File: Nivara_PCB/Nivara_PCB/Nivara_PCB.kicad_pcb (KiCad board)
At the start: 4 copper layers, 98.8 x 81.2 mm, 167 parts, among them CN1 ANALOG_IN, CN2 RELAY, J1 AUXILIAR, K1 SRA-24VDC-CL, K2 SRA-24VDC-CL, P1 NPN_IN, P2 PNP_IN, P3 D_IN, P4 RUN/STOP, P5 NPN_OUT, P6 PNP_OUT, P7 RS485, P8 ANALOG_OUT., Q1 IRLML0040, Q2 AO3407A, Q3 IRLML0040, Q4 AO3407A, Q5 IRLML6402TRPBF-JSM, SW1 SKRPACE010, SW2 SKRPACE010, U1 2.54-2*2, U10 GP8201S-TC50-EW, U11 LK1802, U12 LTV-357T, U13 LTV-357T, U14 LTV-357T, U15 LTV-357T, U16 LTV-357T, U17 LTV-357T, U18 LTV-357T, U19 GP8303-TC50-EW, U2 FUENTE IN, U20 FUENTE EX, U3 ESP32-S3-WROOM-1, U4 AP63200WU, U5 RSM3485ECHT_C2992406, U6 LTV-357T, U7 LTV-357T, U8 LTV-357T, U9 LTV-357T

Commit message: Subida de los cambios.
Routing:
- net VDD: vias 89 -> 94
- net Net-(F2-Pad1): vias 0 -> 12
- net GND: vias 295 -> 302
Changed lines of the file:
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@@
 	)
 	(via
+		(at 178.0762 96.9826)
+		(size 0.6)
+		(drill 0.3)
+		(layers "F.Cu" "B.Cu")
+		(free yes)
+		(net 2)
+	)
+	(via
 		(at 239.118 60.4)
 		(size 0.6)
@@
 	)
 	(via
+		(at 178.7874 96.9572)
+		(size 0.6)
+		(drill 0.3)
+		(layers "F.Cu" "B.Cu")
+		(free yes)
+		(net 2)
+	)
+	(via
 		(at 213.96 57.855)
 		(size 0.6)
@@
 	)
 	(via
+		(at 179.5566 98.3394)
+		(size 0.6)
+		(drill 0.3)
+		(layers "F.Cu" "B.Cu")
+		(free yes)
+		(net 2)
+	)
+	(via
 		(at 228.25 92.51)
 		(size 0.6)
@@
 	)
 	(via
+		(at 180.3146 98.3234)
+		(size 0.6)
+		(drill 0.3)
+		(layers "F.Cu" "B.Cu")
+		(free yes)
+		(net 2)
+	)
+	(via
 		(at 254.403 74.648)
 		(size 0.6)
@@
 	)
 	(via
+		(at 178.1048 97.7392)
+		(size 0.6)
+		(drill 0.3)
+		(layers "F.Cu" "B.Cu")
+		(free yes)
+		(net 2)
+	)
+	(via
 		(at 239.124 59.621)
 		(size 0.6)
@@
 	)
 	(via
+		(at 178.816 97.7138)
+		(size 0.6)
+		(drill 0.3)
+		(layers "F.Cu" "B.Cu")
+		(free yes)
+		(net 2)
+	)
+	(via
 		(at 182.11 49.1)
 		(size 0.6)
@@
 	)
 	(via
+		(at 178.7166 98.3714)
+		(size 0.6)
+		(drill 0.3)
+		(layers "F.Cu" "B.Cu")
+		(free yes)
+		(net 2)
+	)
+	(via
 		(at 187.12 65.34)
 		(size 0.6)
@@
 	)
 	(via
+		(at 257.8502 47.5902)
+		(size 0.6)
+		(drill 0.3)
+		(layers "F.Cu" "B.Cu")
+		(free yes)
+		(net 112)
+	)
+	(via
 		(at 227.5 103)
 		(size 0.6)
@@
 	)
 	(via
+		(at 258.5212 47.5742)
+		(size 0.6)
+		(drill 0.3)
+		(layers "F.Cu" "B.Cu")
+		(free yes)
+		(net 112)
+	)
+	(via
 		(at 234.56 104.6)
 		(size 0.6)
@@
 	)
 	(via
+		(at 255.4852 47.6702)
+		(size 0.6)
+		(drill 0.3)
+		(layers "F.Cu" "B.Cu")
+		(free yes)
+		(net 112)
+	)
+	(via
 		(at 235.36 105.4)
 		(size 0.6)
@@
 	)
 	(via
+		(at 256.3642 47.6382)
+		(size 0.6)
+		(drill 0.3)
+		(layers "F.Cu" "B.Cu")
+		(free yes)
+		(net 112)
+	)
+	(via
 		(at 236.31 103.8)
 		(size 0.6)
@@
 	)
 	(via
+		(at 257.1312 47.6222)
+		(size 0.6)
+		(drill 0.3)
+		(layers "F.Cu" "B.Cu")
+		(free yes)
+		(net 112)
+	)
+	(via
 		(at 226.8 102.2)
 		(size 0.6)
@@
 		(net 112)
 	)
+	(via
+		(at 253.0094 42.4942)
+		(size 0.6)
+		(drill 0.3)
+		(layers "F.Cu" "B.Cu")
+		(free yes)
+		(net 113)
+	)
+	(via
+		(at 256.6162 43.1292)
+		(size 0.6)
+		(drill 0.3)
+		(layers "F.Cu" "B.Cu")
+		(free yes)
+		(net 113)
+	)
+	(via
+		(at 252.3484 45.5198)
+		(size 0.6)
+		(drill 0.3)
+		(layers "F.Cu" "B.Cu")
+		(free yes)
+		(net 113)
+	)
+	(via
+		(at 256.5654 42.2656)
+		(size 0.6)
+		(drill 0.3)
+		(layers "F.Cu" "B.Cu")
+		(free yes)
+		(net 113)
+	)
+	(via
+		(at 252.3372 44.767)
+		(size 0.6)
+		(drill 0.3)
+		(layers "F.Cu" "B.Cu")
+		(free yes)
+		(net 113)
+	)
+	(via
+		(at 253.6444 42.2148)
+		(size 0.6)
+		(drill 0.3)
+		(layers "F.Cu" "B.Cu")
+		(free yes)
+		(net 113)
+	)
+	(via
+		(at 253.0242 44.735)
+		(size 0.6)
+		(drill 0.3)
+		(layers "F.Cu" "B.Cu")
+		(free yes)
+		(net 113)
+	)
+	(via
+		(at 252.3052 44.048)
+		(size 0.6)
+		(drill 0.3)
+		(layers "F.Cu" "B.Cu")
+		(free yes)
+		(net 113)
+	)
+	(via
+		(at 252.9922 44.016)
+		(size 0.6)
+		(drill 0.3)
+		(layers "F.Cu" "B.Cu")
+		(free yes)
+		(net 113)
+	)
+	(via
+		(at 252.3052 43.281)
+		(size 0.6)
+		(drill 0.3)
+		(layers "F.Cu" "B.Cu")
+		(free yes)
+		(net 113)
+	)
+	(via
+		(at 252.3212 42.466)
+		(size 0.6)
+		(drill 0.3)
+		(layers "F.Cu" "B.Cu")
+		(free yes)
+		(net 113)
+	)
+	(via
+		(at 252.9922 43.249)
+		(size 0.6)
+		(drill 0.3)
+		(layers "F.Cu" "B.Cu")
+		(free yes)
+		(net 113)
+	)
 	(segment

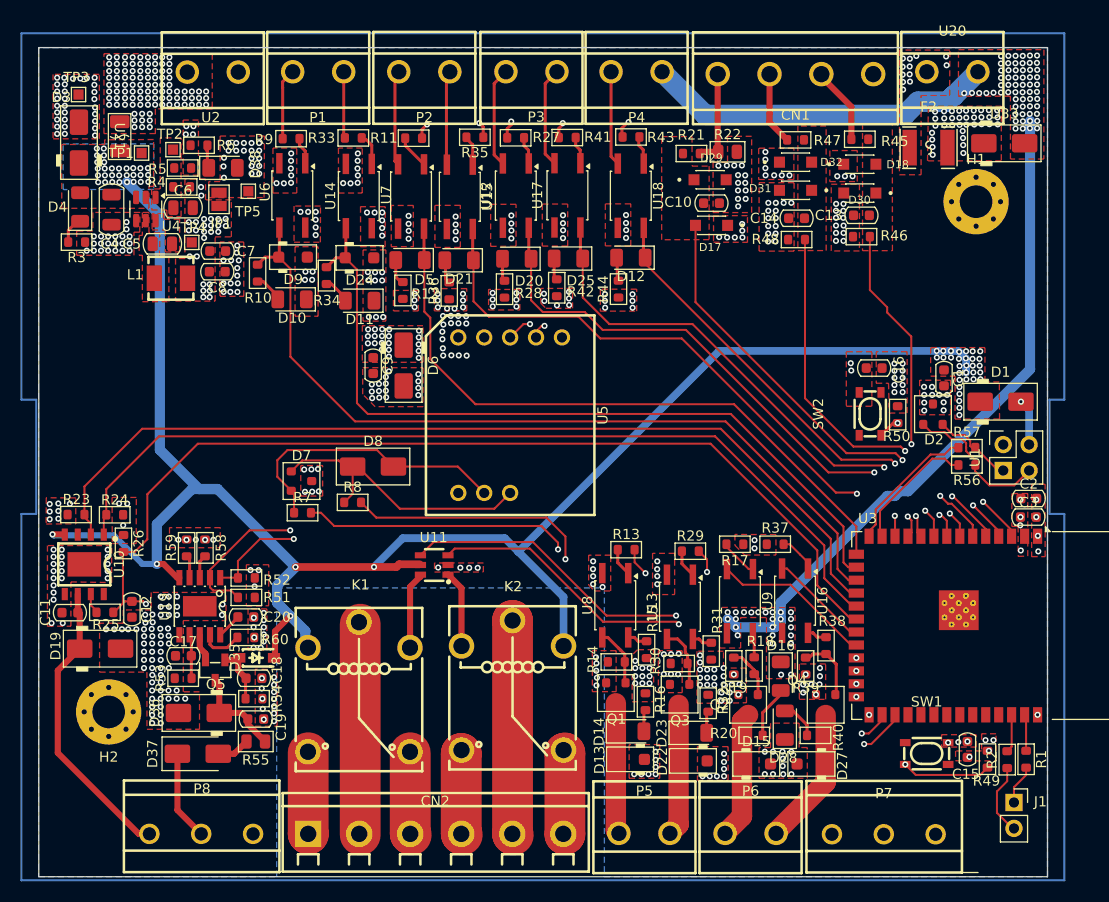
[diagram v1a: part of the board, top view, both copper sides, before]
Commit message: Cambios en las ranuras entre las pistas de los relés, evitando que se crucen las pistas.
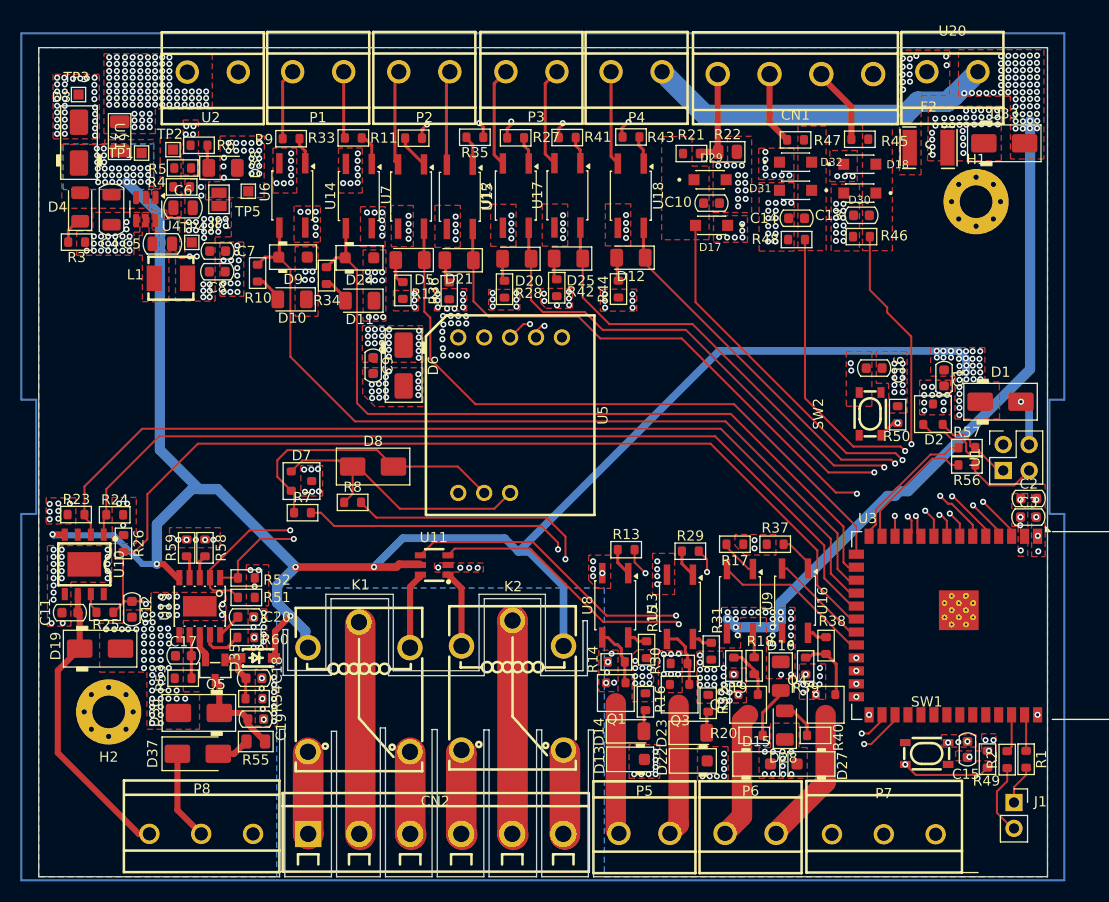
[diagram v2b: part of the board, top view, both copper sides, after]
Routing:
- net VCC: track 179.8 -> 180.4 mm
- net VDD: vias 94 -> 90
- net GND: vias 302 -> 301
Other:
- board size 98.8 x 81.2 mm -> 98.8 x 81.3 mm

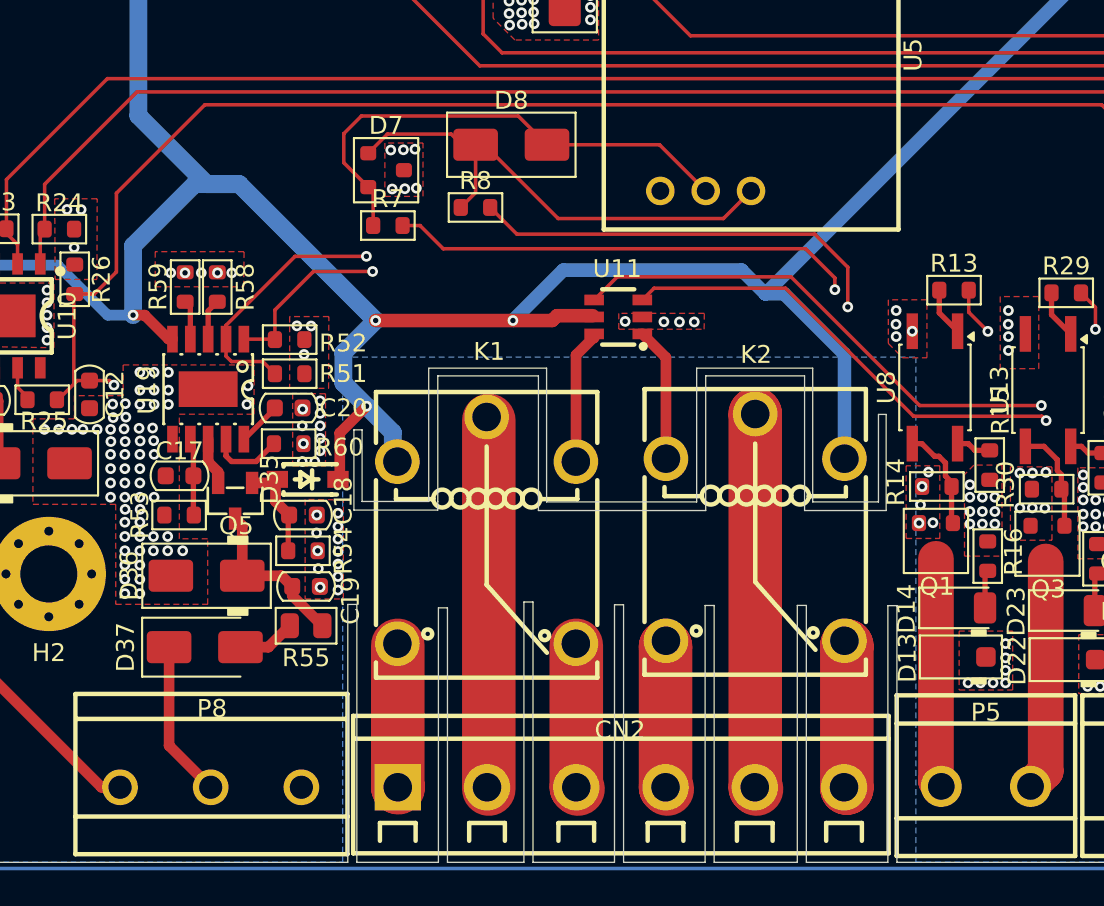
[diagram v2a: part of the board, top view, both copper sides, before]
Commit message: Cambio de capa de las pistas de los relés de las top a bottom y dejada sin soldermask.
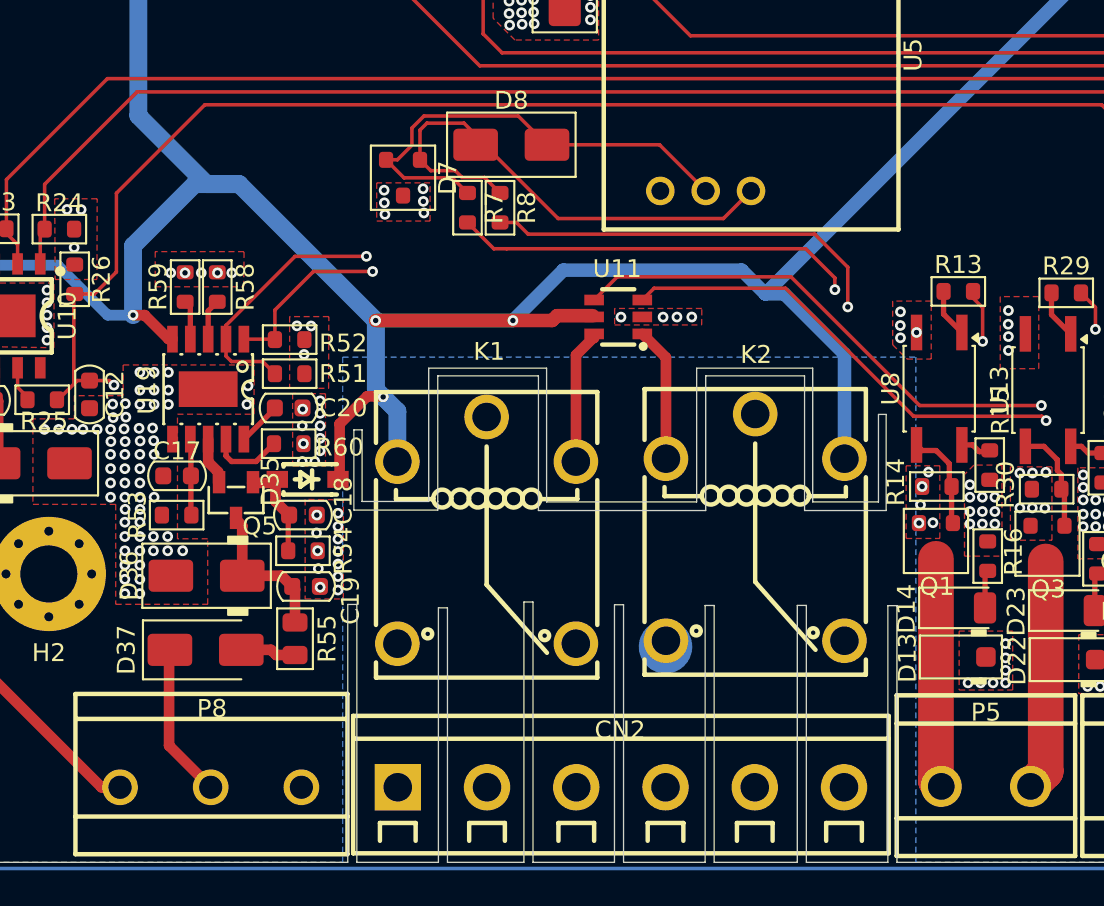
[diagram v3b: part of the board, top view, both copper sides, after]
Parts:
- moved R7 4.57 mm to (198.0, 86.0), turned to -90 degrees
- moved R8 1.37 mm to (199.8, 86.0), turned to -90 degrees
- moved D7 1.04 mm to (194.3, 84.3), turned to -90 degrees
- moved R55 0.96 mm to (188.3, 110.1), turned to -90 degrees
- moved R13 0.25 mm to (225.5, 90.7)
- moved U8 0.25 mm to (224.4, 96.1)
- moved D37 0.16 mm to (183.3, 110.8)
- moved R53 0.14 mm to (181.7, 103.2)
- moved C17 0.14 mm to (181.7, 101.0)
- moved Q5 0.07 mm to (185.0, 102.4)
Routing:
- net VCC: track 180.4 -> 188.1 mm
- net /NIVARA_BOARD/RS485_A+: track 70.5 -> 66.8 mm
- net Net-(D7-A2): track 28.3 -> 26.6 mm
- net Net-(D36-K): track 11.2 -> 10.1 mm
- net /NIVARA_BOARD/RS485_B-: track 69.0 -> 68.1 mm

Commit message: TERMINACIONES Y AJUSTES FINALES
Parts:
- removed the C20 at (187.9, 97.2)
- removed C7, C8: 22uF, PCM_Capacitor_SMD_AKL:C_0603_1608Metric
- removed CN1: ANALOG_IN, EasyEDA:CONN-TH_DB128V-5.0-4P
- removed CN2: RELAY, EasyEDA:CONN-TH_DB126V-5.0-6P-GN
- removed the D10 at (192.5, 66.1)
- removed the D23 at (231.7, 108.5)
- removed the D25 at (219.6, 62.1)
- removed the D28 at (240.8, 107.8)
- removed the D38 at (185.7, 53.2)
- removed the D4 at (171.7, 57.0)
- removed P1: NPN_IN, EasyEDA:CONN-TH_XY126V-5.0-2P
- removed P2: PNP_IN, EasyEDA:CONN-TH_XY126V-5.0-2P
- removed P3: D_IN, EasyEDA:CONN-TH_XY126V-5.0-2P
- removed P4: RUN/STOP, EasyEDA:CONN-TH_XY126V-5.0-2P
- removed P5: NPN_OUT, EasyEDA:CONN-TH_XY126V-5.0-2P
- removed P6: PNP_OUT, EasyEDA:CONN-TH_XY126V-5.0-2P
- removed P7: RS485, EasyEDA:CONN-TH_3P-P5.00_WJ500V-5.08-3P
- removed P8: ANALOG_OUT., EasyEDA:CONN-TH_3P-P5.00_WJ500V-5.08-3P
- removed the R26 at (175.9, 90.0)
- removed the R56 at (258.6, 82.3)
- removed the R57 at (258.6, 80.6)
- removed the R7 at (198.0, 86.0)
- removed SW1, SW2: SKRPACE010, EasyEDA:KEY-SMD_4P-L4.2-W3.2-P2.20-LS4.6
- removed U2: FUENTE IN, EasyEDA:CONN-TH_XY126V-5.0-2P
- removed the U20 at (257.2, 43.8)
- added C19: 1uF, Capacitor_SMD:CP_Elec_4x5.4, F.Cu at (48.9, 83.2)
- added C21: 22uF, PCM_Capacitor_SMD_AKL:C_0805_2012Metric, F.Cu at (47.2, 45.2)
- added C22: 22uF, PCM_Capacitor_SMD_AKL:C_0805_2012Metric, F.Cu at (47.2, 42.1)
- added C4: 10uF, Capacitor_SMD:CP_Elec_4x5.4, F.Cu at (32.8, 37.4)
- added D22: LED, LED_SMD:LED_0603_1608Metric, F.Cu at (76.2, 41.3)
- added D24: LED, LED_SMD:LED_0603_1608Metric, F.Cu at (93.5, 85.8)
- added D26: LED, LED_SMD:LED_0603_1608Metric, F.Cu at (61.0, 45.8)
- added D27: LED, LED_SMD:LED_0603_1608Metric, F.Cu at (70.7, 41.3)
- added D29: LED, LED_SMD:LED_0603_1608Metric, F.Cu at (105.3, 86.4)
- added D30: LED, LED_SMD:LED_0603_1608Metric, F.Cu at (81.6, 41.4)
- added D31: LED, LED_SMD:LED_0603_1608Metric, F.Cu at (87.4, 41.3)
- added D39: SS14, PCM_Diode_SMD_AKL:D_SMA, F.Cu at (123.7, 54.8)
- added D6: LED, LED_SMD:LED_0603_1608Metric, F.Cu at (47.5, 32.7)
- added J10: Bolnera 2P, TerminalBlock_Phoenix:TerminalBlock_Phoenix_MKDS-1,5-2-5.08_1x02_P5.08mm_Horizontal, F.Cu at (46.2, 23.3)
- added J11: Bolnera 2P, TerminalBlock_Phoenix:TerminalBlock_Phoenix_MKDS-1,5-2-5.08_1x02_P5.08mm_Horizontal, F.Cu at (118.8, 23.3)
- added J12: Bolnera 4P, TerminalBlock_Phoenix:TerminalBlock_Phoenix_MKDS-1,5-4-5.08_1x04_P5.08mm_Horizontal, F.Cu at (93.1, 23.9)
- added J13: Bolnera 2P, TerminalBlock_Phoenix:TerminalBlock_Phoenix_MKDS-1,5-2-5.08_1x02_P5.08mm_Horizontal, F.Cu at (87.8, 23.3)
- added J14: Bolnera 6P, TerminalBlock_Phoenix:TerminalBlock_Phoenix_MKDS-1,5-6-5.08_1x06_P5.08mm_Horizontal, F.Cu at (55.2, 96.0)
- added J15: PINHD_2x2_Male, Connector_PinHeader_2.54mm:PinHeader_2x02_P2.54mm_Vertical, F.Cu at (139.0, 47.8)
- added J2: Auxiliares, Connector_PinHeader_2.54mm:PinHeader_1x02_P2.54mm_Vertical, F.Cu at (125.5, 97.4)
- added J3: Bolnera 2P, TerminalBlock_Phoenix:TerminalBlock_Phoenix_MKDS-1,5-2-5.08_1x02_P5.08mm_Horizontal, F.Cu at (56.6, 23.3)
- added J4: Bolnera 3P, TerminalBlock_Phoenix:TerminalBlock_Phoenix_MKDS-1,5-3-5.08_1x03_P5.08mm_Horizontal, F.Cu at (106.7, 96.0)
- added J5: Bolnera 2P, TerminalBlock_Phoenix:TerminalBlock_Phoenix_MKDS-1,5-2-5.08_1x02_P5.08mm_Horizontal, F.Cu at (67.0, 23.3)
- added J6: Bolnera 2P, TerminalBlock_Phoenix:TerminalBlock_Phoenix_MKDS-1,5-2-5.08_1x02_P5.08mm_Horizontal, F.Cu at (77.4, 23.3)
- added J7: Bolnera 2P, TerminalBlock_Phoenix:TerminalBlock_Phoenix_MKDS-1,5-2-5.08_1x02_P5.08mm_Horizontal, F.Cu at (85.9, 96.7)
- added J8: Bolnera 2P, TerminalBlock_Phoenix:TerminalBlock_Phoenix_MKDS-1,5-2-5.08_1x02_P5.08mm_Horizontal, F.Cu at (96.3, 96.6)
- added J9: Bolnera 3P, TerminalBlock_Phoenix:TerminalBlock_Phoenix_MKDS-1,5-3-5.08_1x03_P5.08mm_Horizontal, F.Cu at (39.8, 96.0)
- added JP2: SolderJumper_2_Open, Jumper:SolderJumper-2_P1.3mm_Open_Pad1.0x1.5mm, F.Cu at (59.3, 60.0)
- added JP3: SolderJumper_2_Open, Jumper:SolderJumper-2_P1.3mm_Open_Pad1.0x1.5mm, F.Cu at (59.5, 66.3)
- added LED2: LiteOn_LTST-C19HE1WT, PCM_LED_SMD_AKL:LED_LiteOn_LTST-C19HE1WT, F.Cu at (122.1, 92.9)
- added R1: 33, PCM_Resistor_SMD_AKL:R_0603_1608Metric, F.Cu at (120.3, 62.2)
- added R2: 33, PCM_Resistor_SMD_AKL:R_0603_1608Metric, F.Cu at (120.2, 60.4)
- added R30: 10k, PCM_Resistor_SMD_AKL:R_0603_1608Metric, F.Cu at (38.3, 66.9)
- added R31: 1.5k, PCM_Resistor_SMD_AKL:R_0603_1608Metric, F.Cu at (72.8, 70.3)
- added R32: 1.5k, PCM_Resistor_SMD_AKL:R_0603_1608Metric, F.Cu at (63.6, 70.5)
- added R4: 20, PCM_Resistor_SMD_AKL:R_0603_1608Metric, F.Cu at (122.1, 89.6)
- added R5: 20, PCM_Resistor_SMD_AKL:R_0603_1608Metric, F.Cu at (122.1, 87.5)
- added R65: 5.1K, PCM_Resistor_SMD_AKL:R_0603_1608Metric, F.Cu at (140.5, 30.4)
- added R66: 500, PCM_Resistor_SMD_AKL:R_0603_1608Metric, F.Cu at (142.4, 30.4)
- added R67: 5.1K, PCM_Resistor_SMD_AKL:R_0603_1608Metric, F.Cu at (138.0, 30.4)
- added R8: 1.5k, PCM_Resistor_SMD_AKL:R_0603_1608Metric, F.Cu at (31.5, 25.9)
- added SW3: SW_Push, Button_Switch_SMD:SW_SPST_PTS810, F.Cu at (110.9, 88.3)
- added SW4: SW_Push, Button_Switch_SMD:SW_SPST_PTS810, F.Cu at (110.9, 56.0)
- C11: value 0.1uF -> 100nF
- C14: footprint PCM_Capacitor_SMD_AKL:C_0603_1608Metric -> PCM_Capacitor_SMD_AKL:C_0805_2012Metric
- C18, C9: footprint PCM_Capacitor_SMD_AKL:C_0603_1608Metric -> Capacitor_SMD:CP_Elec_4x5.4
- C2: value 22uF -> 2.2uF
- C20: renamed from C19; value 0.1uF -> 100nF
- D1: value SS12 -> LED; footprint PCM_Diode_SMD_AKL:D_SMA -> LED_SMD:LED_0603_1608Metric
- D11, D12, D14, D16, D20, D21: value IR26-21C_L110_TR8 -> LED; footprint LED_SMD:LED_1206_3216Metric -> LED_SMD:LED_0603_1608Metric
- D5: value IR26-21C_L110_TR8 -> LED_R; footprint LED_SMD:LED_1206_3216Metric -> LED_SMD:LED_0603_1608Metric
- F3: renamed from U21; value ~ -> Resettable fuse
- J1: value AUXILIAR -> Conn_02x02_Counter_Clockwise; footprint Connector_PinSocket_2.54mm:PinSocket_1x02_P2.54mm_Vertical -> Connector_PinSocket_2.54mm:PinSocket_2x02_P2.54mm_Vertical
- L1: value CXP0420-6R8M-AG(6.8UH) -> HCMA-0420-6R8-M
- R12: renamed from R8; value R_0603 -> 120
- R26: renamed from R22; value 145 -> 147
- R3: value 1k2 -> 20
- U1: value 2.54-2*2 -> GT-USB-7010ASV; footprint Connector_PinSocket_2.54mm:PinSocket_2x02_P2.54mm_Vertical -> EasyEDA:USB-C-SMD_G-SWITCH_GT-USB-7010ASV
- U5: renamed from U3; footprint RF_Module:ESP32-S3-WROOM-1 -> RF_Module:ESP32-S3-WROOM-1U
- moved D5 175.4 mm to (31.6, 30.4), turned to -90 degrees
- moved D12 161.1 mm to (65.9, 41.2)
- moved J1 150.4 mm to (124.0, 58.6), turned to 90 degrees
- moved D21 149.3 mm to (59.7, 70.4)
- moved TP1 147.2 mm to (31.7, 33.0)
- moved R55 146.8 mm to (115.7, 87.4), turned to 180 degrees
- moved D11 145.8 mm to (54.7, 46.0)
- moved R12 145.7 mm to (55.9, 63.2)
- moved C20 145.2 mm to (46.3, 79.6)
- moved C15 144.5 mm to (115.7, 89.2), turned to 180 degrees
- moved R58 143.7 mm to (47.9, 63.4), turned to -90 degrees
- moved R46 143.2 mm to (102.5, 85.3), turned to -90 degrees
- moved U5 143.2 mm to (118.7, 76.5)
- moved R63 143.2 mm to (48.4, 76.7), turned to -90 degrees
- moved D37 142.9 mm to (42.6, 81.7), turned to 90 degrees
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- renumbered D9 to D10, D29 to D18, D22 to D23, D24 to D25, D27 to D28, D18 to D32, D30 to D33, D32 to D34, D31 to D35, D35 to D36, D36 to D37, D37 to D38, D33 to D4, D6 to D7, D7 to D9, F2 to F1, K2 to K1, K1 to K2, R5 to R10, R6 to R11, R9 to R13, R10 to R14, R11 to R15, R12 to R16, R13 to R17, R14 to R18, R15 to R19, R16 to R20, R17 to R21, R18 to R22, R19 to R23, R20 to R24, R21 to R25, R23 to R27, R24 to R28, R25 to R29, R27 to R33, R28 to R34, R29 to R35, R30 to R36, R31 to R37, R32 to R38, R33 to R39, R34 to R40, R35 to R41, R36 to R42, R37 to R43, R38 to R44, R39 to R45, R40 to R46, R41 to R47, R42 to R48, R43 to R49, R44 to R50, R45 to R51, R46 to R52, R47 to R53, R48 to R54, R49 to R55, R50 to R56, R59 to R57, R51 to R58, R58 to R59, R1 to R6, R52 to R60, R60 to R61, R53 to R62, R54 to R63, R55 to R64, R2 to R7, R4 to R9, U8 to U10, U9 to U11, U10 to U12, U11 to U13, U12 to U14, U13 to U15, U14 to U16, U15 to U17, U16 to U18, U17 to U19, U18 to U20, U19 to U21, U4 to U6, U5 to U7, U6 to U8, U7 to U9
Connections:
- C14 pad 1: /NIVARA_BOARD/A_0-10_IN/A_V_OUT -> GND
- C14 pad 2: GND -> /NIVARA_BOARD/A_0-10_IN/A_V_OUT
- C15 pad 1: GND -> +3.3V
- C15 pad 2: +3.3V -> GND
- C16 pad 1: GND -> +3.3V
- C16 pad 2: +3.3V -> GND
- C18 pad 1: Net-(D35-A) -> Net-(U21-V5V)
- D1 pad 1: VCC -> Net-(D1-K)
- D1 pad 2: Net-(D1-A) -> +5V
- D12 pad 1: /NIVARA_BOARD/RUN_STOP/D_OUT -> /NIVARA_BOARD/PNP_IN_1/PNP_OUT
- D16 pad 1: Earth -> Net-(D16-K)
- D16 pad 2: Net-(D16-A) -> /NIVARA_BOARD/PNP_OUT_1
- D2 pad 1: /D+ -> /USB/D-
- D2 pad 2: /D- -> /USB/D+
- D20 pad 1: /NIVARA_BOARD/D_IN_1/D_OUT -> Net-(D20-K)
- D20 pad 2: Net-(D20-A) -> VCC
- D21 pad 1: /NIVARA_BOARD/PNP_IN_2/PNP_OUT -> Net-(D21-K)
- D21 pad 2: Net-(D21-A) -> VCC
- D36 pad 2: Net-(D35-A) -> Net-(D36-A)
- D5 pad 1: /NIVARA_BOARD/PNP_IN_1/PNP_OUT -> Net-(D5-K)
- D5 pad 2: Net-(D5-A) -> VCC
- D8 pad 1: Net-(D7-A1) -> /NIVARA_BOARD/RS485_A+
- D8 pad 2: Net-(D7-A2) -> /NIVARA_BOARD/RS485_B-
- D9 pad 1: Net-(D7-A1) -> /NIVARA_BOARD/RS485_A+
- D9 pad 2: Net-(D7-A2) -> /NIVARA_BOARD/RS485_B-
- J1 pad 1: /NIVARA_BOARD/AUX_1 -> GND
- J1 pad 2: /NIVARA_BOARD/AUX_2 -> /USB/D+
- Q5 pad 1: Net-(D35-A) -> Net-(D36-A)
- R12 pad 1: Net-(D7-A1) -> Net-(JP2-A)
- R12 pad 2: /NIVARA_BOARD/RS485_B- -> Net-(JP3-A)
- R14 pad 2: Net-(D10-A) -> Net-(D11-A)
- R16 pad 2: Net-(D5-A) -> Net-(D12-A)
- R24 pad 1: /NIVARA_BOARD/PNP_OUT_1 -> Net-(D16-K)
- R24 pad 2: Net-(D16-A) -> Earth
- R3 pad 1: GND -> Net-(LED2-R)
- R3 pad 2: Net-(D4-K) -> Net-(U5-MTCK/GPIO39/CLK_OUT3/SUBSPICS1)
- R34 pad 2: Net-(D20-A) -> Net-(D22-A)
- R40 pad 2: Net-(D11-A) -> Net-(D26-A)
- R42 pad 2: Net-(D21-A) -> Net-(D27-A)
- R46 pad 1: /NIVARA_BOARD/PNP_OUT_2 -> Net-(D29-K)
- R46 pad 2: Net-(D28-A) -> Earth
- R50 pad 2: Net-(D12-A) -> Net-(D31-A)
- R63 pad 1: Net-(D35-A) -> Net-(D36-A)
- U1 pad 1: GND -> GND1
- U1 pad 2: /D- -> GND1
- U1 pad 3: Net-(D1-A) -> GND1
- U1 pad 4: /D+ -> GND1
- U21 pad 10: Net-(U19-V5V) -> Net-(U21-V5V)
- U5 pad 13: /NIVARA_BOARD/USB_D+ -> /NIVARA_BOARD/USB_D-
- U5 pad 14: /NIVARA_BOARD/USB_D- -> /NIVARA_BOARD/USB_D+
- U5 pad 25: /NIVARA_BOARD/A_I_OUT/SDA_C -> /NIVARA_BOARD/A_I_OUT/SCLK_C
- U5 pad 26: /NIVARA_BOARD/A_I_OUT/SCLK_C -> /NIVARA_BOARD/A_I_OUT/SDA_C
- U5 pad 32: unconnected-(U3-MTCK/GPIO39/CLK_OUT3/SUBSPICS1-Pad32) -> Net-(U5-MTCK/GPIO39/CLK_OUT3/SUBSPICS1)
- U5 pad 33: unconnected-(U3-MTDO/GPIO40/CLK_OUT2-Pad33) -> Net-(U5-MTDO/GPIO40/CLK_OUT2)
- U5 pad 34: unconnected-(U3-MTDI/GPIO41/CLK_OUT1-Pad34) -> Net-(U5-MTDI/GPIO41/CLK_OUT1)
- U7 pad 8: Net-(D7-A1) -> /NIVARA_BOARD/RS485_B-
- U7 pad 9: Net-(D7-A2) -> /NIVARA_BOARD/RS485_A+
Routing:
- net Net-(D7-A1): track 28.8 -> 0.00 mm
- net Net-(D7-A2): track 26.6 -> 0.00 mm
- net Net-(U1-DN1): track 0.00 -> 24.8 mm
- net /D+: track 14.6 -> 28.6 mm
- net /USB/D-: track 0.00 -> 13.7 mm
- net VCC: track 188.1 -> 199.7 mm, vias 66 -> 56
- net Net-(D36-A): track 0.00 -> 11.0 mm
- net +5V: track 0.00 -> 9.25 mm, vias 0 -> 7
- net /USB/D+: track 0.00 -> 8.50 mm
- net /D-: track 8.10 -> 0.00 mm
- net Net-(U21-V5V): track 0.00 -> 7.44 mm
- net Net-(D37-K): track 10.1 -> 17.4 mm
- net +3.3V: track 215.7 -> 223.0 mm, vias 144 -> 147
- net Net-(LED2-B): track 0.00 -> 7.16 mm
- net /NIVARA_BOARD/BUTTON/BUTTON_PIN: track 15.4 -> 8.77 mm, vias 2 -> 1
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- added copper zone on B.Cu, net +5V
- added copper zone on F.Cu, net GND1
- added copper zone on In2.Cu, net VDD
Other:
- board size 98.8 x 81.3 mm -> 120 x 79.5 mm
